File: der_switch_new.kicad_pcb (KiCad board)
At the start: 2 copper layers, 1 part, among them U1 KSZ9477S

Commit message: add ports
Signed-off-by: Oleksij Rempel <linux@rempel-privat.de>
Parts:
- added C1: 22 uF, Capacitor_SMD:C_0402_1005Metric_Pad0.74x0.62mm_HandSolder, F.Cu at (127.0, 63.5)
- added C10: 0.1 uF, Capacitor_SMD:C_0402_1005Metric_Pad0.74x0.62mm_HandSolder, F.Cu at (111.5, 57.6)
- added C11: 0.1 uF, Capacitor_SMD:C_0402_1005Metric_Pad0.74x0.62mm_HandSolder, F.Cu at (96.0, 86.9)
- added C12: 0.1 uF, Capacitor_SMD:C_0402_1005Metric_Pad0.74x0.62mm_HandSolder, F.Cu at (103.8, 69.3)
- added C13: 0.1 uF, Capacitor_SMD:C_0402_1005Metric_Pad0.74x0.62mm_HandSolder, F.Cu at (103.8, 75.2)
- added C14: 0.1 uF, Capacitor_SMD:C_0402_1005Metric_Pad0.74x0.62mm_HandSolder, F.Cu at (88.2, 69.3)
- added C15: 22 uF, Capacitor_SMD:C_0402_1005Metric_Pad0.74x0.62mm_HandSolder, F.Cu at (88.2, 75.2)
- added C16: 0.1 uF, Capacitor_SMD:C_0402_1005Metric_Pad0.74x0.62mm_HandSolder, F.Cu at (111.5, 63.5)
- added C17: 0.1 uF, Capacitor_SMD:C_0402_1005Metric_Pad0.74x0.62mm_HandSolder, F.Cu at (119.2, 63.5)
- added C18: 0.1 uF, Capacitor_SMD:C_0402_1005Metric_Pad0.74x0.62mm_HandSolder, F.Cu at (103.8, 63.5)
- added C19: 0.1 uF, Capacitor_SMD:C_0402_1005Metric_Pad0.74x0.62mm_HandSolder, F.Cu at (96.0, 63.5)
- added C2: 22 uF, Capacitor_SMD:C_0402_1005Metric_Pad0.74x0.62mm_HandSolder, F.Cu at (111.5, 69.3)
- added C20: 0.1 uF, Capacitor_SMD:C_0402_1005Metric_Pad0.74x0.62mm_HandSolder, F.Cu at (96.0, 57.6)
- added C21: 0.1 uF, Capacitor_SMD:C_0402_1005Metric_Pad0.74x0.62mm_HandSolder, F.Cu at (88.2, 81.0)
- added C22: 0.1 uF, Capacitor_SMD:C_0402_1005Metric_Pad0.74x0.62mm_HandSolder, F.Cu at (88.2, 86.9)
- added C23: 0.1 uF, Capacitor_SMD:C_0402_1005Metric_Pad0.74x0.62mm_HandSolder, F.Cu at (111.5, 86.9)
- added C24: 0.1 uF, Capacitor_SMD:C_0402_1005Metric_Pad0.74x0.62mm_HandSolder, F.Cu at (127.0, 57.6)
- added C25: 0.1 uF, Capacitor_SMD:C_0402_1005Metric_Pad0.74x0.62mm_HandSolder, F.Cu at (119.2, 57.6)
- added C26: 0.1 uF, Capacitor_SMD:C_0402_1005Metric_Pad0.74x0.62mm_HandSolder, F.Cu at (103.8, 57.6)
- added C27: 0.1 uF, Capacitor_SMD:C_0402_1005Metric_Pad0.74x0.62mm_HandSolder, F.Cu at (119.2, 81.0)
- added C28: 0.1 uF, Capacitor_SMD:C_0402_1005Metric_Pad0.74x0.62mm_HandSolder, F.Cu at (88.2, 63.5)
- added C29: 0.1 uF, Capacitor_SMD:C_0402_1005Metric_Pad0.74x0.62mm_HandSolder, F.Cu at (96.0, 69.3)
- added C3: 0.1 uF, Capacitor_SMD:C_0402_1005Metric_Pad0.74x0.62mm_HandSolder, F.Cu at (103.8, 81.0)
- added C30: 22 uF, Capacitor_SMD:C_0402_1005Metric_Pad0.74x0.62mm_HandSolder, F.Cu at (103.8, 86.9)
- added C31: 0.1 uF, Capacitor_SMD:C_0402_1005Metric_Pad0.74x0.62mm_HandSolder, F.Cu at (142.5, 76.2)
- added C32: 0.1 uF, Capacitor_SMD:C_0402_1005Metric_Pad0.74x0.62mm_HandSolder, F.Cu at (134.8, 69.3)
- added C33: 0.1 uF, Capacitor_SMD:C_0402_1005Metric_Pad0.74x0.62mm_HandSolder, F.Cu at (111.5, 75.2)
- added C34: 0.1 uF, Capacitor_SMD:C_0402_1005Metric_Pad0.74x0.62mm_HandSolder, F.Cu at (88.2, 57.6)
- added C35: 10 uF, Capacitor_SMD:C_0402_1005Metric_Pad0.74x0.62mm_HandSolder, F.Cu at (142.5, 57.6)
- added C36: 0.1 uF, Capacitor_SMD:C_0402_1005Metric_Pad0.74x0.62mm_HandSolder, F.Cu at (119.2, 75.2)
- added C37: 0.1 uF, Capacitor_SMD:C_0402_1005Metric_Pad0.74x0.62mm_HandSolder, F.Cu at (134.8, 63.5)
- added C38: 22 uF, Capacitor_SMD:C_0402_1005Metric_Pad0.74x0.62mm_HandSolder, F.Cu at (96.0, 81.0)
- added C39: 0.1 uF, Capacitor_SMD:C_0402_1005Metric_Pad0.74x0.62mm_HandSolder, F.Cu at (152.4, 38.1)
- added C4: 0.1 uF, Capacitor_SMD:C_0402_1005Metric_Pad0.74x0.62mm_HandSolder, F.Cu at (127.0, 69.3)
- added C40: 0.1 uF, Capacitor_SMD:C_0402_1005Metric_Pad0.74x0.62mm_HandSolder, F.Cu at (152.4, 36.1)
- added C41: 0.1 uF, Capacitor_SMD:C_0402_1005Metric_Pad0.74x0.62mm_HandSolder, F.Cu at (155.6, 36.1)
- added C42: 0.1 uF, Capacitor_SMD:C_0402_1005Metric_Pad0.74x0.62mm_HandSolder, F.Cu at (182.7, 18.3)
- added C43: 0.1 uF, Capacitor_SMD:C_0402_1005Metric_Pad0.74x0.62mm_HandSolder, F.Cu at (160.3, 66.5)
- added C44: 0.1 uF, Capacitor_SMD:C_0402_1005Metric_Pad0.74x0.62mm_HandSolder, F.Cu at (155.6, 72.3)
- added C45: 0.1 uF, Capacitor_SMD:C_0402_1005Metric_Pad0.74x0.62mm_HandSolder, F.Cu at (165.1, 63.5)
- added C46: 0.1 uF, Capacitor_SMD:C_0402_1005Metric_Pad0.74x0.62mm_HandSolder, F.Cu at (160.3, 68.4)
- added C47: 0.1 uF, Capacitor_SMD:C_0402_1005Metric_Pad0.74x0.62mm_HandSolder, F.Cu at (158.8, 72.3)
- added C48: 0.1 uF, Capacitor_SMD:C_0402_1005Metric_Pad0.74x0.62mm_HandSolder, F.Cu at (165.1, 65.5)
- added C49: 0.1 uF, Capacitor_SMD:C_0402_1005Metric_Pad0.74x0.62mm_HandSolder, F.Cu at (168.3, 63.5)
- added C5: 0.1 uF, Capacitor_SMD:C_0402_1005Metric_Pad0.74x0.62mm_HandSolder, F.Cu at (111.5, 81.0)
- added C50: 0.1 uF, Capacitor_SMD:C_0402_1005Metric_Pad0.74x0.62mm_HandSolder, F.Cu at (155.6, 74.3)
- added C51: 0.1 uF, Capacitor_SMD:C_0402_1005Metric_Pad0.74x0.62mm_HandSolder, F.Cu at (165.1, 127.0)
- added C52: 0.1 uF, Capacitor_SMD:C_0402_1005Metric_Pad0.74x0.62mm_HandSolder, F.Cu at (160.3, 129.9)
- added C53: 0.1 uF, Capacitor_SMD:C_0402_1005Metric_Pad0.74x0.62mm_HandSolder, F.Cu at (155.6, 133.9)
- added C54: 0.1 uF, Capacitor_SMD:C_0402_1005Metric_Pad0.74x0.62mm_HandSolder, F.Cu at (165.1, 125.0)
- added C55: 0.1 uF, Capacitor_SMD:C_0402_1005Metric_Pad0.74x0.62mm_HandSolder, F.Cu at (168.3, 125.0)
- added C56: 0.1 uF, Capacitor_SMD:C_0402_1005Metric_Pad0.74x0.62mm_HandSolder, F.Cu at (155.6, 135.8)
- added C57: 0.1 uF, Capacitor_SMD:C_0402_1005Metric_Pad0.74x0.62mm_HandSolder, F.Cu at (160.3, 128.0)
- added C58: 0.1 uF, Capacitor_SMD:C_0402_1005Metric_Pad0.74x0.62mm_HandSolder, F.Cu at (158.8, 133.9)
- added C6: 0.1 uF, Capacitor_SMD:C_0402_1005Metric_Pad0.74x0.62mm_HandSolder, F.Cu at (134.8, 57.6)
- added C7: 0.1 uF, Capacitor_SMD:C_0402_1005Metric_Pad0.74x0.62mm_HandSolder, F.Cu at (127.0, 75.2)
- added C8: 0.1 uF, Capacitor_SMD:C_0402_1005Metric_Pad0.74x0.62mm_HandSolder, F.Cu at (96.0, 75.2)
- added C9: 0.1 uF, Capacitor_SMD:C_0402_1005Metric_Pad0.74x0.62mm_HandSolder, F.Cu at (119.2, 69.3)
- added J1: JK0654219, Connector_RJ:RJ45_Pulse_JK0654219NL_Horizontal, F.Cu at (226.1, 25.4)
- added J2: JK0654219, Connector_RJ:RJ45_Pulse_JK0654219NL_Horizontal, F.Cu at (226.1, 50.8)
- added J3: JK0654219, Connector_RJ:RJ45_Pulse_JK0654219NL_Horizontal, F.Cu at (226.1, 77.5)
- added J4: JK0654219, Connector_RJ:RJ45_Pulse_JK0654219NL_Horizontal, F.Cu at (226.1, 102.4)
- added J5: JK0654219, Connector_RJ:RJ45_Pulse_JK0654219NL_Horizontal, F.Cu at (226.1, 127.0)
- added R1: 330, Resistor_SMD:R_0805_2012Metric_Pad1.20x1.40mm_HandSolder, F.Cu at (156.4, 125.5)
- added R10: 330, Resistor_SMD:R_0805_2012Metric_Pad1.20x1.40mm_HandSolder, F.Cu at (156.4, 128.5)
- added R2: 330, Resistor_SMD:R_0805_2012Metric_Pad1.20x1.40mm_HandSolder, F.Cu at (183.5, 15.8)
- added R3: 330, Resistor_SMD:R_0805_2012Metric_Pad1.20x1.40mm_HandSolder, F.Cu at (148.4, 36.6)
- added R4: 330, Resistor_SMD:R_0805_2012Metric_Pad1.20x1.40mm_HandSolder, F.Cu at (156.4, 64.0)
- added R5: 330, Resistor_SMD:R_0805_2012Metric_Pad1.20x1.40mm_HandSolder, F.Cu at (156.4, 69.9)
- added R6: 330, Resistor_SMD:R_0805_2012Metric_Pad1.20x1.40mm_HandSolder, F.Cu at (156.4, 66.9)
- added R7: 330, Resistor_SMD:R_0805_2012Metric_Pad1.20x1.40mm_HandSolder, F.Cu at (161.1, 64.0)
- added R8: 330, Resistor_SMD:R_0805_2012Metric_Pad1.20x1.40mm_HandSolder, F.Cu at (156.4, 131.4)
- added R9: 330, Resistor_SMD:R_0805_2012Metric_Pad1.20x1.40mm_HandSolder, F.Cu at (161.1, 125.5)
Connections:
- net no_connect_(U1-Pad102) renamed /ethernet ports/P5_LED0
- net no_connect_(U1-Pad103) renamed /ethernet ports/P5_LED1
- net no_connect_(U1-Pad112) renamed /ethernet ports/P5_A_P
- net no_connect_(U1-Pad113) renamed /ethernet ports/P5_A_M
- net no_connect_(U1-Pad115) renamed /ethernet ports/P5_B_P
- net no_connect_(U1-Pad116) renamed /ethernet ports/P5_B_M
- net no_connect_(U1-Pad117) renamed /ethernet ports/P5_C_P
- net no_connect_(U1-Pad118) renamed /ethernet ports/P5_C_M
- net no_connect_(U1-Pad120) renamed /ethernet ports/P5_D_P
- net no_connect_(U1-Pad121) renamed /ethernet ports/P5_D_M
- U1 pad 1: no_connect_(U1-Pad1) -> /ethernet ports/ethernet_ports_1_2/P1_A_P
- U1 pad 10: no_connect_(U1-Pad10) -> +2V5
- U1 pad 104: no_connect_(U1-Pad104) -> +1V2
- U1 pad 105: no_connect_(U1-Pad105) -> /ethernet ports/ethernet_ports_1_2/P1_LED0
- U1 pad 106: no_connect_(U1-Pad106) -> /ethernet ports/ethernet_ports_1_2/P1_LED1
- U1 pad 107: no_connect_(U1-Pad107) -> GND
- U1 pad 109: no_connect_(U1-Pad109) -> GND
- U1 pad 11: no_connect_(U1-Pad11) -> +1V2
- U1 pad 110: no_connect_(U1-Pad110) -> +1V2
- U1 pad 111: no_connect_(U1-Pad111) -> +2V5
- U1 pad 114: no_connect_(U1-Pad114) -> +1V2
- U1 pad 119: no_connect_(U1-Pad119) -> +1V2
- U1 pad 12: no_connect_(U1-Pad12) -> /ethernet ports/ethernet_ports_1_2/P2_A_P
- U1 pad 122: no_connect_(U1-Pad122) -> +2V5
- U1 pad 123: no_connect_(U1-Pad123) -> GND
- U1 pad 124: no_connect_(U1-Pad124) -> +1V2
- U1 pad 128: no_connect_(U1-Pad128) -> +2V5
- U1 pad 13: no_connect_(U1-Pad13) -> /ethernet ports/ethernet_ports_1_2/P2_A_M
- U1 pad 14: no_connect_(U1-Pad14) -> +1V2
- U1 pad 15: no_connect_(U1-Pad15) -> /ethernet ports/ethernet_ports_1_2/P2_B_P
- U1 pad 16: no_connect_(U1-Pad16) -> /ethernet ports/ethernet_ports_1_2/P2_B_M
- U1 pad 17: no_connect_(U1-Pad17) -> /ethernet ports/ethernet_ports_1_2/P2_C_P
- U1 pad 18: no_connect_(U1-Pad18) -> /ethernet ports/ethernet_ports_1_2/P2_C_M
- U1 pad 19: no_connect_(U1-Pad19) -> +1V2
- U1 pad 2: no_connect_(U1-Pad2) -> /ethernet ports/ethernet_ports_1_2/P1_A_M
- U1 pad 20: no_connect_(U1-Pad20) -> /ethernet ports/ethernet_ports_1_2/P2_D_P
- U1 pad 21: no_connect_(U1-Pad21) -> /ethernet ports/ethernet_ports_1_2/P2_D_M
- U1 pad 22: no_connect_(U1-Pad22) -> +2V5
- U1 pad 23: no_connect_(U1-Pad23) -> +1V2
- U1 pad 24: no_connect_(U1-Pad24) -> /ethernet ports/ethernet_ports_3_4/P3_A_P
- U1 pad 25: no_connect_(U1-Pad25) -> /ethernet ports/ethernet_ports_3_4/P3_A_M
- U1 pad 26: no_connect_(U1-Pad26) -> /ethernet ports/ethernet_ports_3_4/P3_B_P
- U1 pad 27: no_connect_(U1-Pad27) -> /ethernet ports/ethernet_ports_3_4/P3_B_M
- U1 pad 28: no_connect_(U1-Pad28) -> /ethernet ports/ethernet_ports_3_4/P3_C_P
- U1 pad 29: no_connect_(U1-Pad29) -> /ethernet ports/ethernet_ports_3_4/P3_C_M
- U1 pad 3: no_connect_(U1-Pad3) -> +1V2
- U1 pad 30: no_connect_(U1-Pad30) -> +1V2
- U1 pad 31: no_connect_(U1-Pad31) -> /ethernet ports/ethernet_ports_3_4/P3_D_P
- U1 pad 32: no_connect_(U1-Pad32) -> /ethernet ports/ethernet_ports_3_4/P3_D_M
- U1 pad 33: no_connect_(U1-Pad33) -> +2V5
- U1 pad 34: no_connect_(U1-Pad34) -> /ethernet ports/ethernet_ports_3_4/P4_A_P
- U1 pad 35: no_connect_(U1-Pad35) -> /ethernet ports/ethernet_ports_3_4/P4_A_M
- U1 pad 36: no_connect_(U1-Pad36) -> +1V2
- U1 pad 37: no_connect_(U1-Pad37) -> /ethernet ports/ethernet_ports_3_4/P4_B_P
- U1 pad 38: no_connect_(U1-Pad38) -> /ethernet ports/ethernet_ports_3_4/P4_B_M
- U1 pad 39: no_connect_(U1-Pad39) -> /ethernet ports/ethernet_ports_3_4/P4_C_P
- U1 pad 4: no_connect_(U1-Pad4) -> /ethernet ports/ethernet_ports_1_2/P1_B_P
- U1 pad 40: no_connect_(U1-Pad40) -> /ethernet ports/ethernet_ports_3_4/P4_C_M
- U1 pad 41: no_connect_(U1-Pad41) -> +1V2
- U1 pad 42: no_connect_(U1-Pad42) -> /ethernet ports/ethernet_ports_3_4/P4_D_P
- U1 pad 43: no_connect_(U1-Pad43) -> /ethernet ports/ethernet_ports_3_4/P4_D_M
- U1 pad 44: no_connect_(U1-Pad44) -> +2V5
- U1 pad 45: no_connect_(U1-Pad45) -> +1V2
- U1 pad 46: no_connect_(U1-Pad46) -> GND
- U1 pad 47: no_connect_(U1-Pad47) -> GND
- U1 pad 5: no_connect_(U1-Pad5) -> /ethernet ports/ethernet_ports_1_2/P1_B_M
- U1 pad 56: no_connect_(U1-Pad56) -> +1V2
- U1 pad 6: no_connect_(U1-Pad6) -> /ethernet ports/ethernet_ports_1_2/P1_C_P
- U1 pad 61: no_connect_(U1-Pad61) -> +3V3
- U1 pad 66: no_connect_(U1-Pad66) -> +1V2
- U1 pad 68: no_connect_(U1-Pad68) -> +3V3
- U1 pad 69: no_connect_(U1-Pad69) -> GND
- U1 pad 7: no_connect_(U1-Pad7) -> /ethernet ports/ethernet_ports_1_2/P1_C_M
- U1 pad 70: no_connect_(U1-Pad70) -> +1V2
- U1 pad 71: no_connect_(U1-Pad71) -> +1V2
- U1 pad 72: no_connect_(U1-Pad72) -> +2V5
- U1 pad 75: no_connect_(U1-Pad75) -> GND
- U1 pad 77: no_connect_(U1-Pad77) -> GND
- U1 pad 8: no_connect_(U1-Pad8) -> /ethernet ports/ethernet_ports_1_2/P1_D_P
- U1 pad 80: no_connect_(U1-Pad80) -> GND
- U1 pad 83: no_connect_(U1-Pad83) -> +2V5
- U1 pad 84: no_connect_(U1-Pad84) -> +1V2
- U1 pad 85: no_connect_(U1-Pad85) -> /ethernet ports/ethernet_ports_3_4/P4_LED0
- U1 pad 86: no_connect_(U1-Pad86) -> /ethernet ports/ethernet_ports_3_4/P4_LED1
- U1 pad 87: no_connect_(U1-Pad87) -> +1V2
- U1 pad 88: no_connect_(U1-Pad88) -> /ethernet ports/ethernet_ports_3_4/P3_LED0
- U1 pad 89: no_connect_(U1-Pad89) -> /ethernet ports/ethernet_ports_3_4/P3_LED1
- U1 pad 9: no_connect_(U1-Pad9) -> /ethernet ports/ethernet_ports_1_2/P1_D_M
- U1 pad 91: no_connect_(U1-Pad91) -> /ethernet ports/ethernet_ports_1_2/P2_LED0
- U1 pad 92: no_connect_(U1-Pad92) -> /ethernet ports/ethernet_ports_1_2/P2_LED1
- U1 pad 99: no_connect_(U1-Pad99) -> +3V3

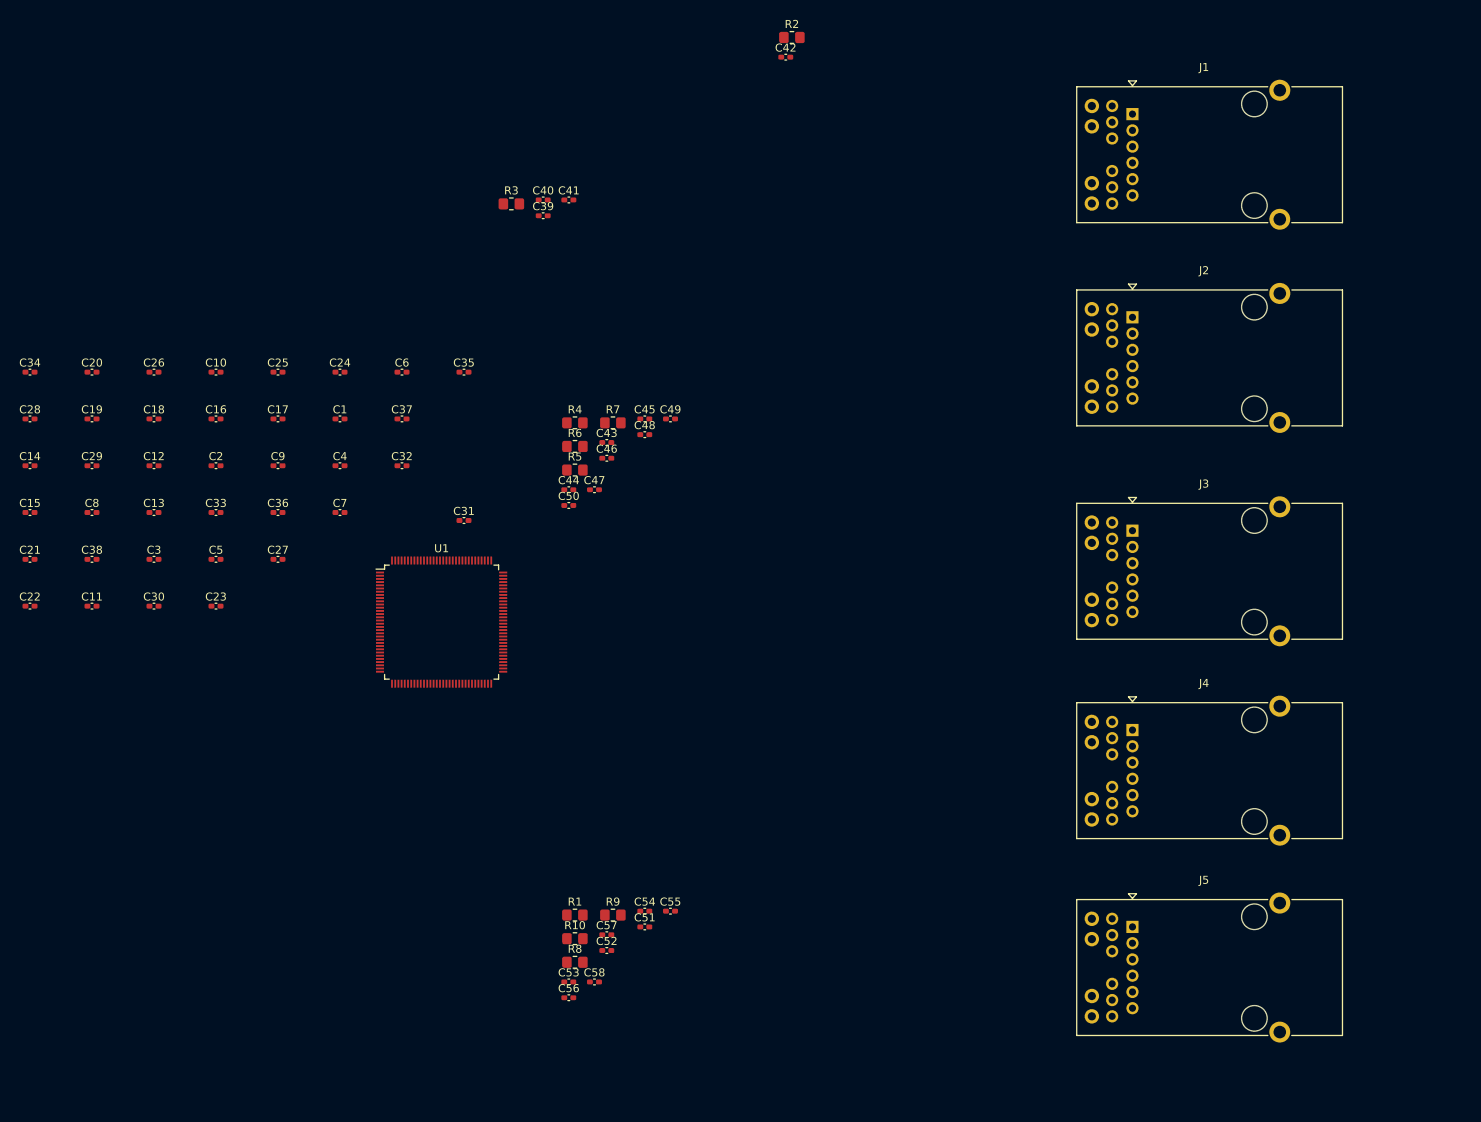
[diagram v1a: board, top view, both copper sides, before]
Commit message: add TQFP-128_14x14mm_P0.4mm_EP10x10mm_ThermalVias footprint
and assign it to the ksz chip

Signed-off-by: Oleksij Rempel <linux@rempel-privat.de>
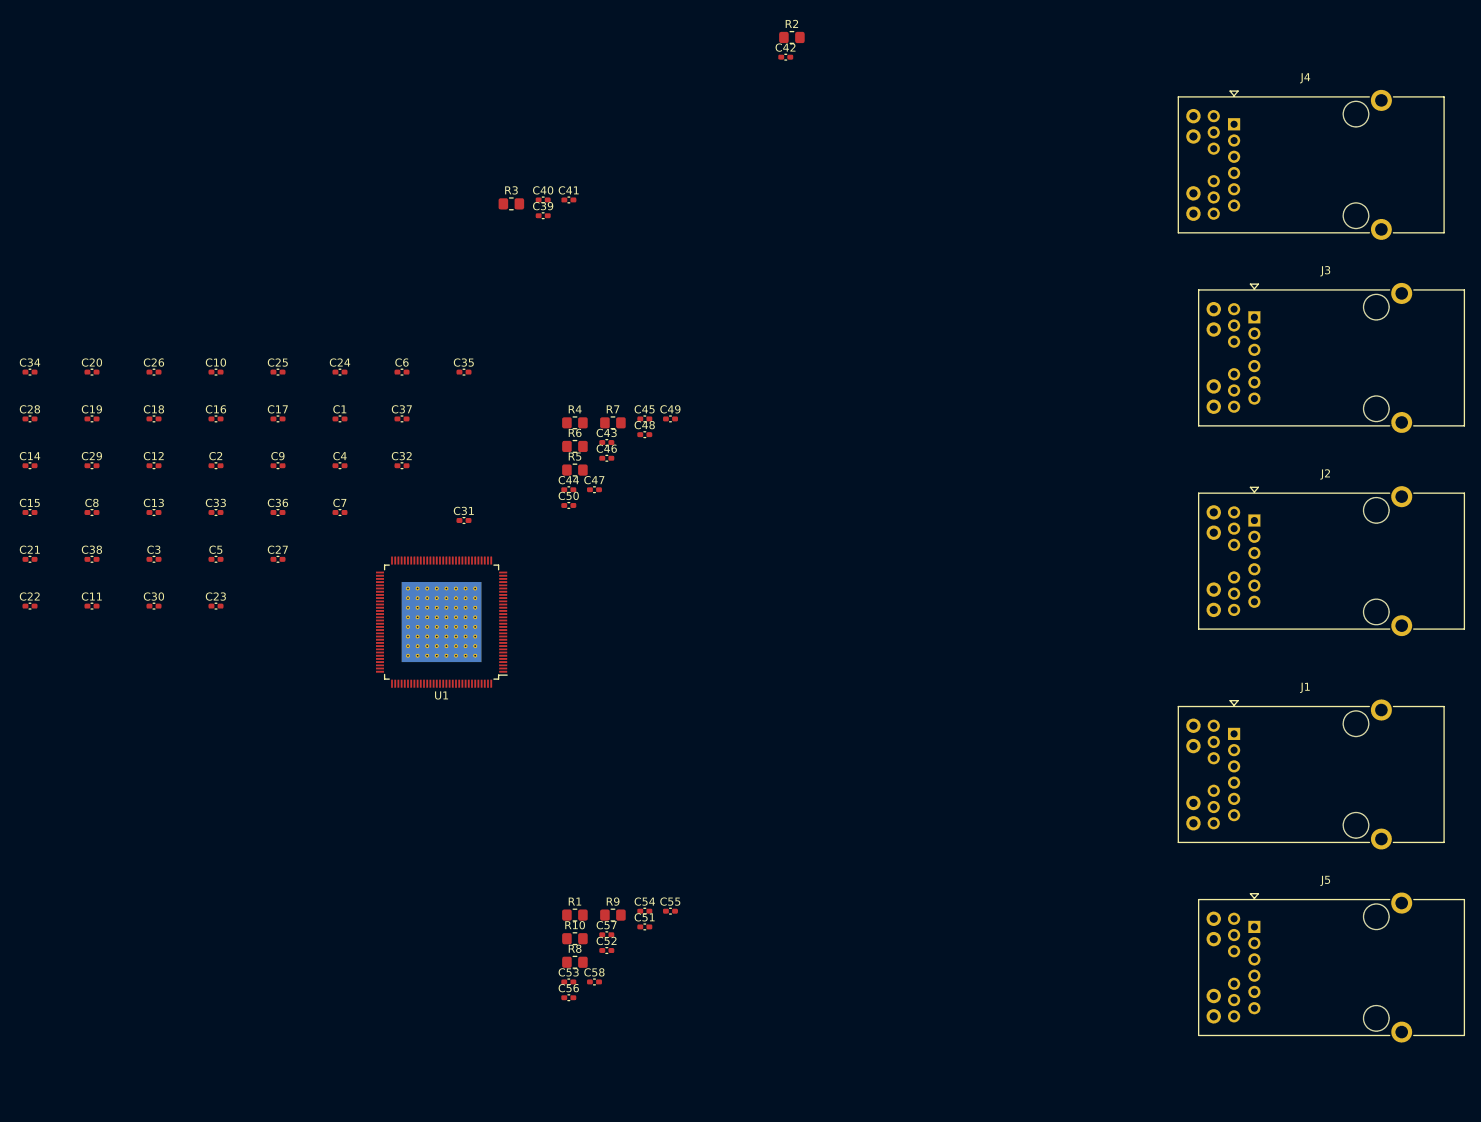
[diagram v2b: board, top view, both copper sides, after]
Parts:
- U1: footprint Package_QFP:TQFP-128_14x14mm_P0.4mm -> footprints:TQFP-128_14x14mm_P0.4mm_EP10x10mm_ThermalVias
- moved J1 78.5 mm to (238.8, 102.9)
- moved J4 76.8 mm to (238.8, 26.7)
- moved J3 30.7 mm to (241.3, 50.8)
- moved J2 29.6 mm to (241.3, 76.2)
- moved J5 15.2 mm to (241.3, 127.0)
- turned U1 to 180 degrees
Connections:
- J5 pad 10: /ethernet ports/P1_A_M -> /ethernet ports/P5_A_M
- J5 pad 11: /ethernet ports/P1_A_P -> /ethernet ports/P5_A_P
- J5 pad 13: /ethernet ports/P1_LED1 -> /ethernet ports/P5_LED1
- J5 pad 15: /ethernet ports/P1_LED0 -> /ethernet ports/P5_LED0
- J5 pad 2: /ethernet ports/P1_C_M -> /ethernet ports/P5_C_M
- J5 pad 3: /ethernet ports/P1_C_P -> /ethernet ports/P5_C_P
- J5 pad 4: /ethernet ports/P1_B_P -> /ethernet ports/P5_B_P
- J5 pad 5: /ethernet ports/P1_B_M -> /ethernet ports/P5_B_M
- J5 pad 8: /ethernet ports/P1_D_P -> /ethernet ports/P5_D_P
- J5 pad 9: /ethernet ports/P1_D_M -> /ethernet ports/P5_D_M
